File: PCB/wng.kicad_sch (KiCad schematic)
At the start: 12 parts, among them Q2 2N3904, Q5 2N3904, Q6 2N3904, X4 WNS

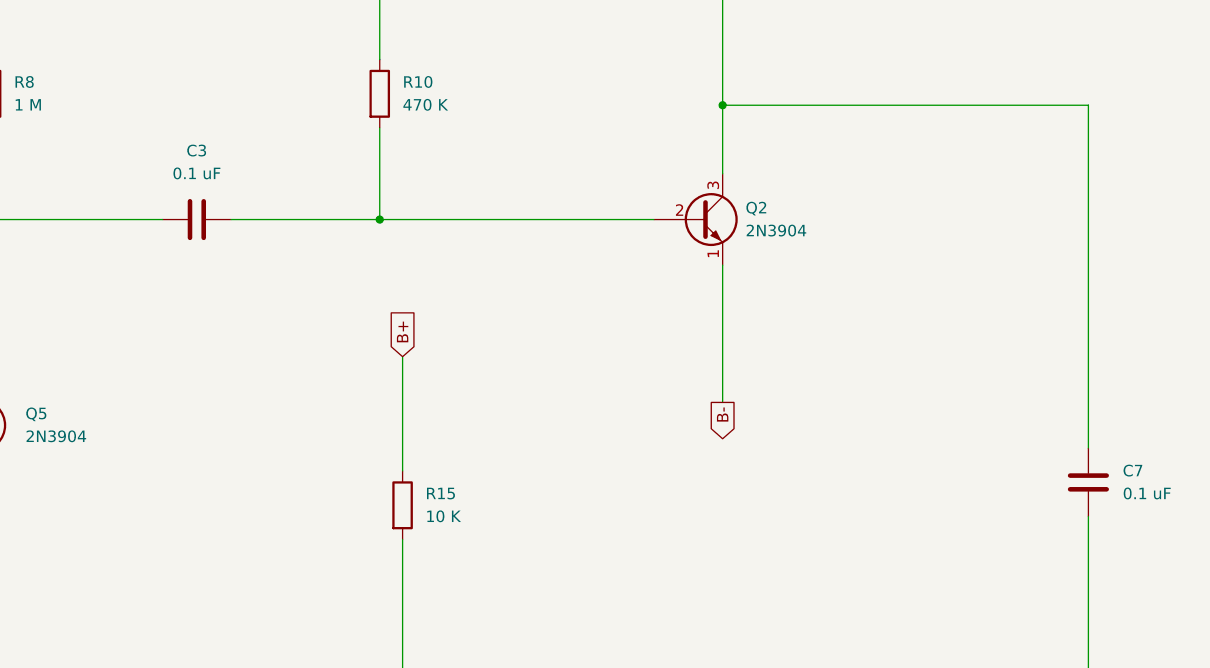
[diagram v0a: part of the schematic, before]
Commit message: Change TO-92 transistors to wide package to avoid shorting during soldering
Added B- hole for speaker
Added more vias to shorten traces
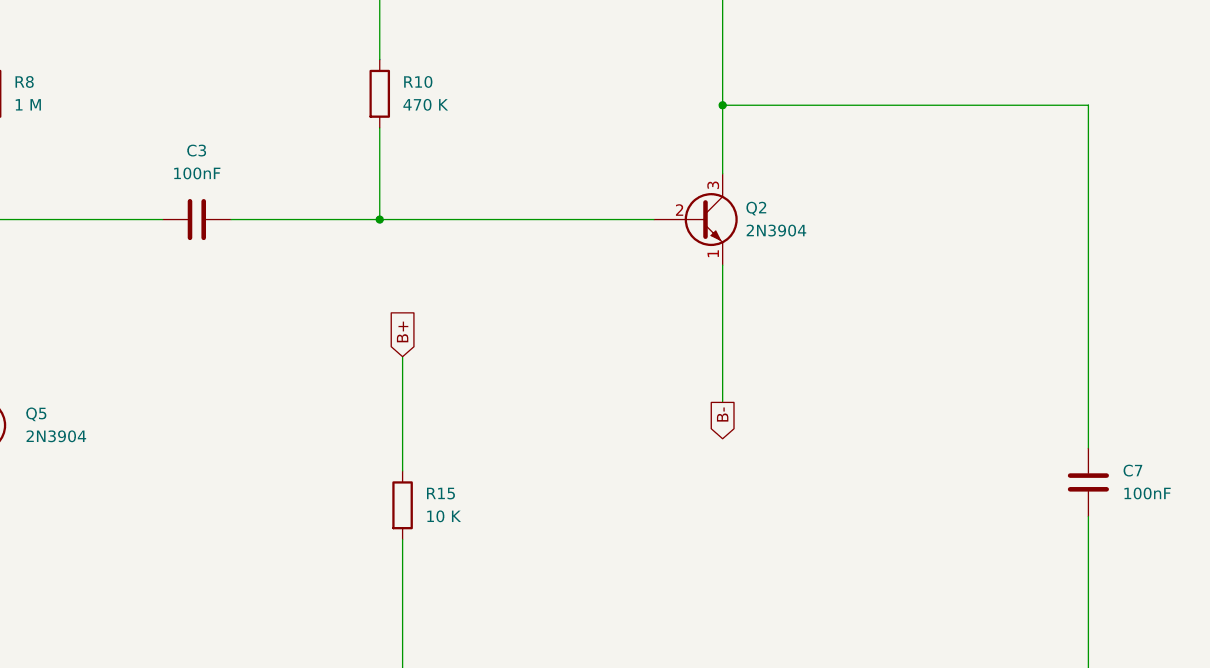
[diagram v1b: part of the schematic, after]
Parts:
- C3, C7: value 0.1 uF -> 100nF
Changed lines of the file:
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@@
 			)
 		)
-		(property "Value" "0.1 uF"
+		(property "Value" "100nF"
 			(at 129.54 71.12 90)
 			(show_name no)
@@
 		(fields_autoplaced yes)
 		(property "Reference" "C7"
-			(at 232.41 104.14 0)
-			(show_name no)
-			(do_not_autoplace no)
-			(effects
-				(font
-					(size 1.27 1.27)
-				)
-				(justify left)
-			)
-		)
-		(property "Value" "0.1 uF"
-			(at 232.41 106.68 0)
-			(show_name no)
-			(do_not_autoplace no)
+			(at 232.41 104.1399 0)
+			(show_name no)
+			(do_not_autoplace no)
+			(effects
+				(font
+					(size 1.27 1.27)
+				)
+				(justify left)
+			)
+		)
+		(property "Value" "100nF"
+			(at 232.41 106.6799 0)
+			(show_name no)
+			(do_not_autoplace no)

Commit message: Necessary Changes to Schematic and PCB
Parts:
- Q2, Q5, Q6: footprint Package_TO_SOT_THT:TO-92_Inline -> Package_TO_SOT_THT:TO-92_Inline_Wide
- X4: footprint Connector_PinHeader_2.00mm:PinHeader_1x01_P2.00mm_Vertical -> Connector_PinSocket_2.54mm:PinSocket_1x01_P2.54mm_Vertical
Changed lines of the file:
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@@
 			)
 		)
-		(property "Footprint" "Connector_PinHeader_2.00mm:PinHeader_1x01_P2.00mm_Vertical"
+		(property "Footprint" "Connector_PinSocket_2.54mm:PinSocket_1x01_P2.54mm_Vertical"
 			(at 63.5 127 0)
 			(hide yes)
@@
 			)
 		)
-		(property "Footprint" "Package_TO_SOT_THT:TO-92_Inline"
+		(property "Footprint" "Package_TO_SOT_THT:TO-92_Inline_Wide"
 			(at 190.5 78.105 0)
 			(hide yes)
@@
 			)
 		)
-		(property "Footprint" "Package_TO_SOT_THT:TO-92_Inline"
+		(property "Footprint" "Package_TO_SOT_THT:TO-92_Inline_Wide"
 			(at 109.22 97.155 0)
 			(hide yes)
@@
 			)
 		)
-		(property "Footprint" "Package_TO_SOT_THT:TO-92_Inline"
+		(property "Footprint" "Package_TO_SOT_THT:TO-92_Inline_Wide"
 			(at 115.57 153.035 0)
 			(hide yes)

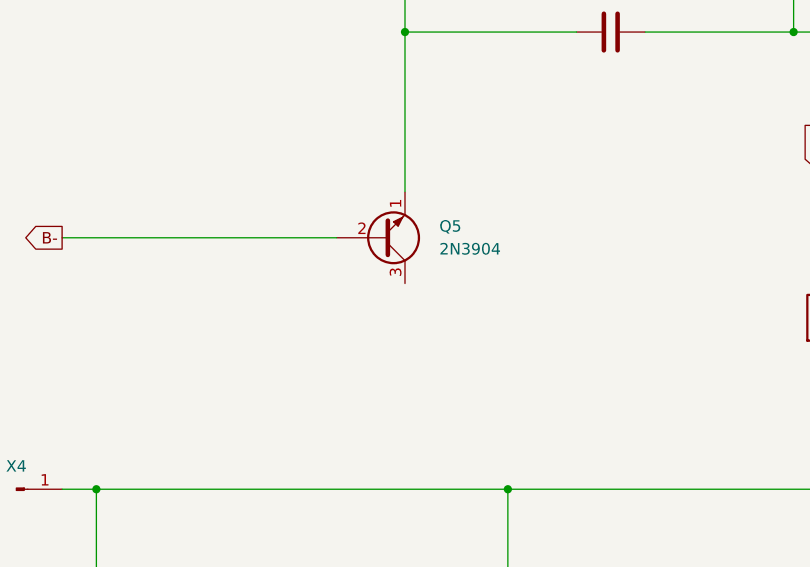
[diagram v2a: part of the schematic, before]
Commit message: Fixed grave mistake (Q10 position swapped)
Tom forgot to mirror Q10, swapping the emitter and collectors of Q10
Changed all the footprints of electrolytic caps to 5mm (i didnt find a single cap in my parts bin rated for 25V that was 4mm diameter)
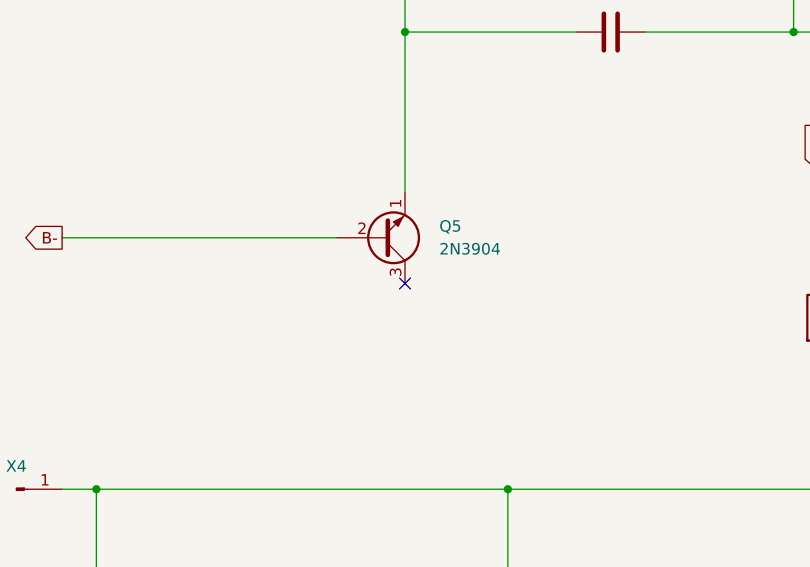
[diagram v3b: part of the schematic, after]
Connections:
- no-connect marks 0 -> 1
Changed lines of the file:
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@@
 		(color 0 0 0 0)
+	)
+	(no_connect
+		(at 106.68 104.14)
 	)
 	(wire

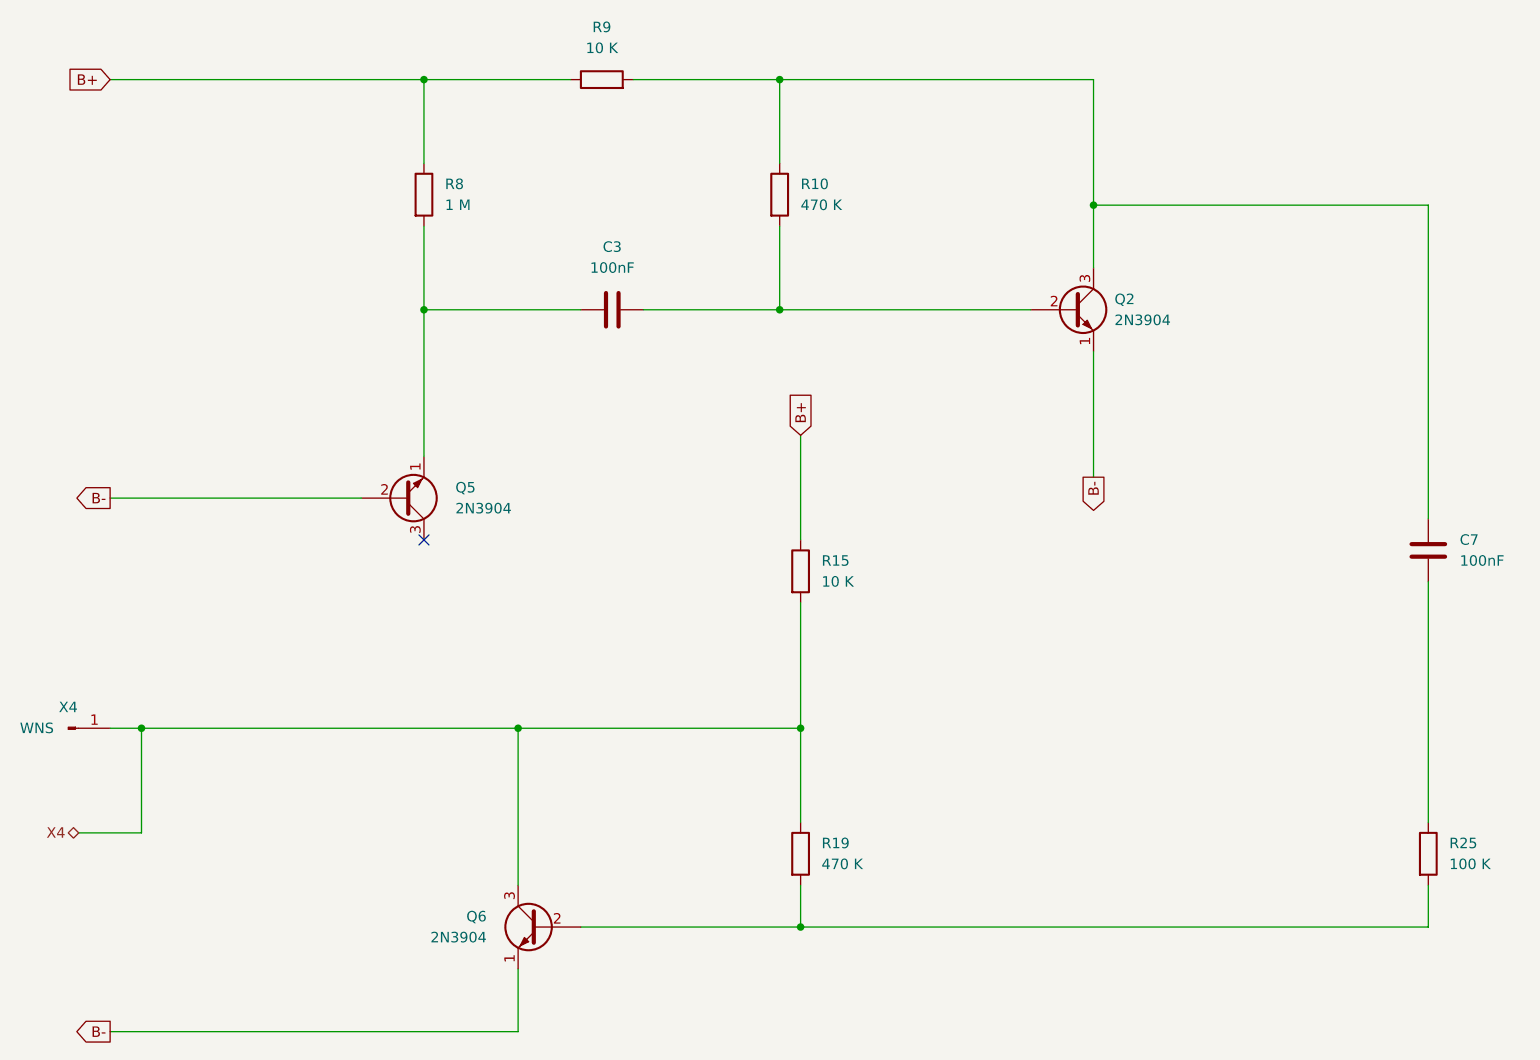
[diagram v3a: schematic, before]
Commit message: Final Update
Move power pins closer to filter caps
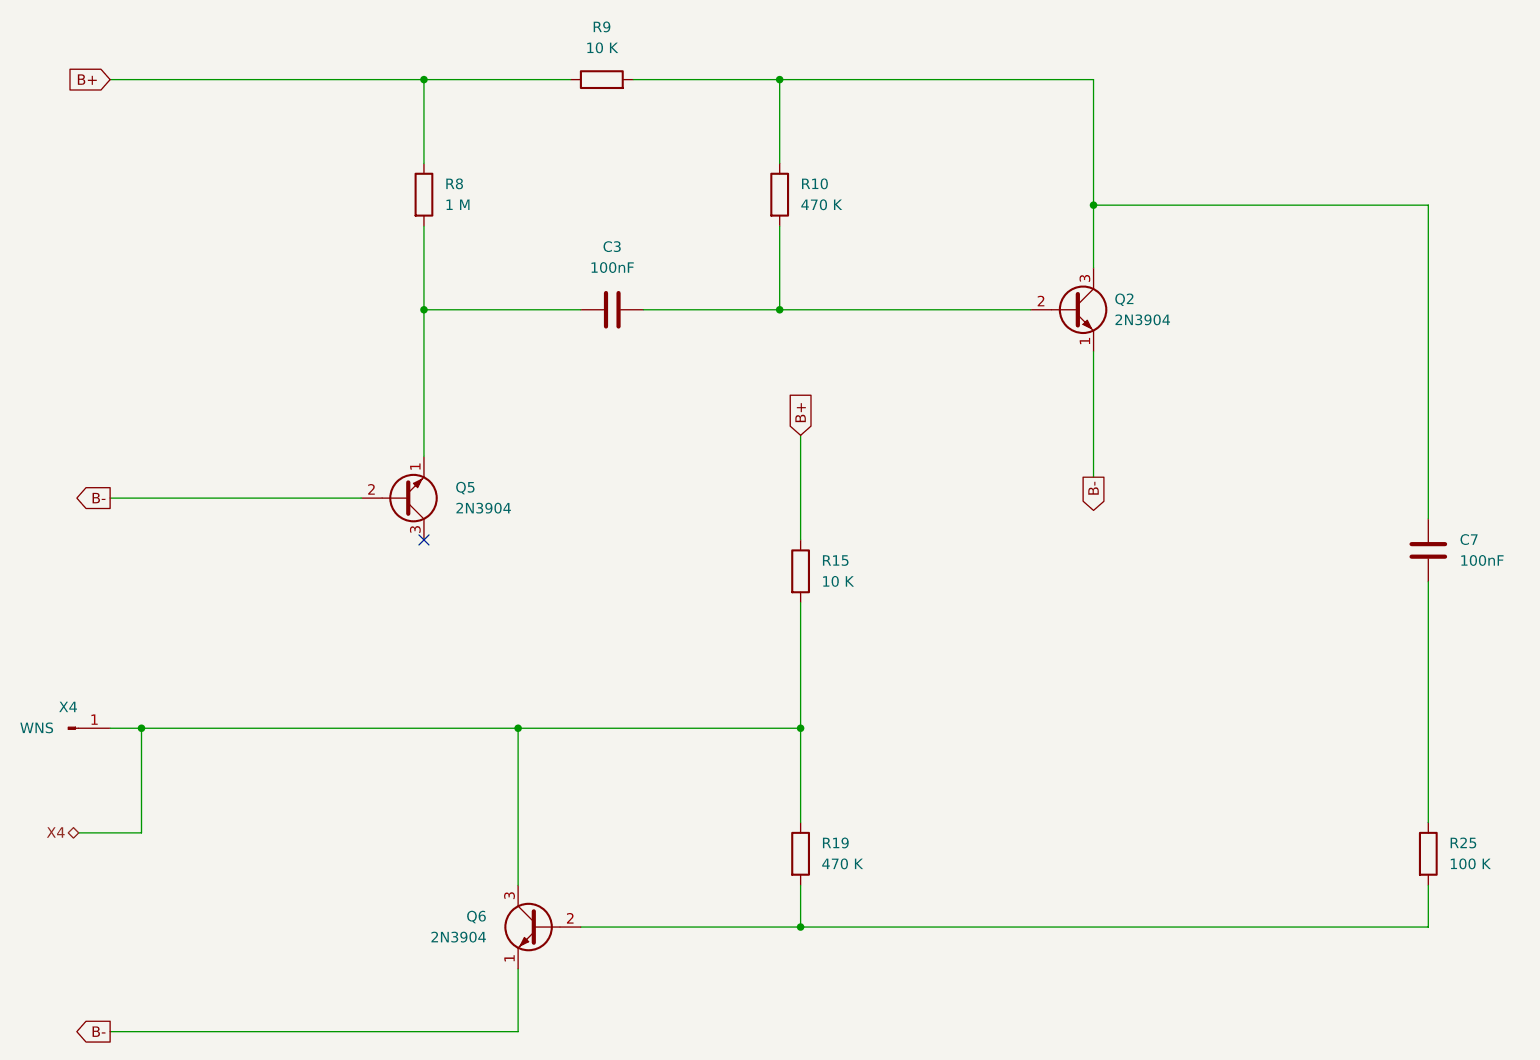
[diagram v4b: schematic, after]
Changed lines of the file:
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@@
 		(fields_autoplaced yes)
 		(property "Reference" "Q2"
-			(at 190.5 74.93 0)
+			(at 190.5 74.9299 0)
 			(show_name no)
 			(do_not_autoplace no)
@@
 		)
 		(property "Value" "2N3904"
-			(at 190.5 77.47 0)
+			(at 190.5 77.4699 0)
 			(show_name no)
 			(do_not_autoplace no)
@@
 			)
 		)
-		(property "Description" ""
+		(property "Description" "0.2A Ic, 40V Vce, Small Signal NPN Transistor, TO-92"
+			(at 185.42 76.2 0)
+			(hide yes)
+			(show_name no)
+			(do_not_autoplace no)
+			(effects
+				(font
+					(size 1.27 1.27)
+				)
+			)
+		)
+		(property "Sim.Device" "NPN"
+			(at 185.42 76.2 0)
+			(hide yes)
+			(show_name no)
+			(do_not_autoplace no)
+			(effects
+				(font
+					(size 1.27 1.27)
+				)
+			)
+		)
+		(property "Sim.Pins" "1=E 2=B 3=C"
 			(at 185.42 76.2 0)
 			(hide yes)
@@
 			)
 		)
-		(property "Description" ""
+		(property "Description" "0.2A Ic, 40V Vce, Small Signal NPN Transistor, TO-92"
+			(at 104.14 99.06 0)
+			(hide yes)
+			(show_name no)
+			(do_not_autoplace no)
+			(effects
+				(font
+					(size 1.27 1.27)
+				)
+			)
+		)
+		(property "Sim.Device" "NPN"
+			(at 104.14 99.06 0)
+			(hide yes)
+			(show_name no)
+			(do_not_autoplace no)
+			(effects
+				(font
+					(size 1.27 1.27)
+				)
+			)
+		)
+		(property "Sim.Pins" "1=E 2=B 3=C"
 			(at 104.14 99.06 0)
 			(hide yes)
@@
 			)
 		)
-		(property "Description" ""
+		(property "Description" "0.2A Ic, 40V Vce, Small Signal NPN Transistor, TO-92"
 			(at 120.65 151.13 0)
 			(hide yes)
+			(show_name no)
+			(do_not_autoplace no)
+			(effects
+				(font
+					(size 1.27 1.27)
+				)
+			)
+		)
+		(property "Sim.Device" "NPN"
+			(at 120.65 151.13 0)
+			(hide yes)
+			(show_name no)
+			(do_not_autoplace no)
+			(effects
+				(font
+					(size 1.27 1.27)
+				)
+			)
+		)
+		(property "Sim.Pins" "1=E 2=B 3=C"
+			(at 120.65 151.13 0)
+			(hide yes)
